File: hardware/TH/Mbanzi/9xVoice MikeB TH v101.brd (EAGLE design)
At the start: 78.1 x 45 mm, 82 parts, among them IC1 ATMEGA328P, IC2 LE33CZ, IC3 LM386N, IC4 LM7805CT, Q1 12MHz, T1 BSS295, T2 BSS295

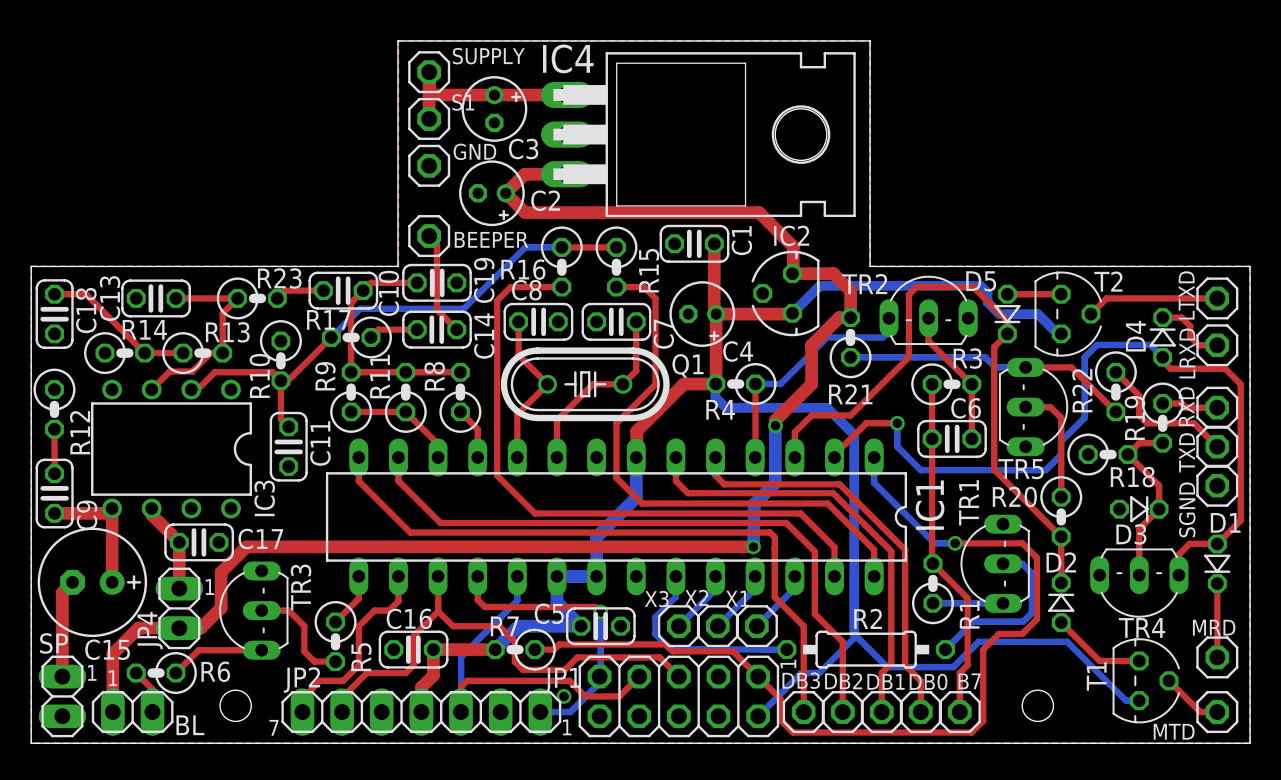
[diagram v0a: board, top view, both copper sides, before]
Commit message: Added Eagle 6.3.0 files for all my versions of the designs
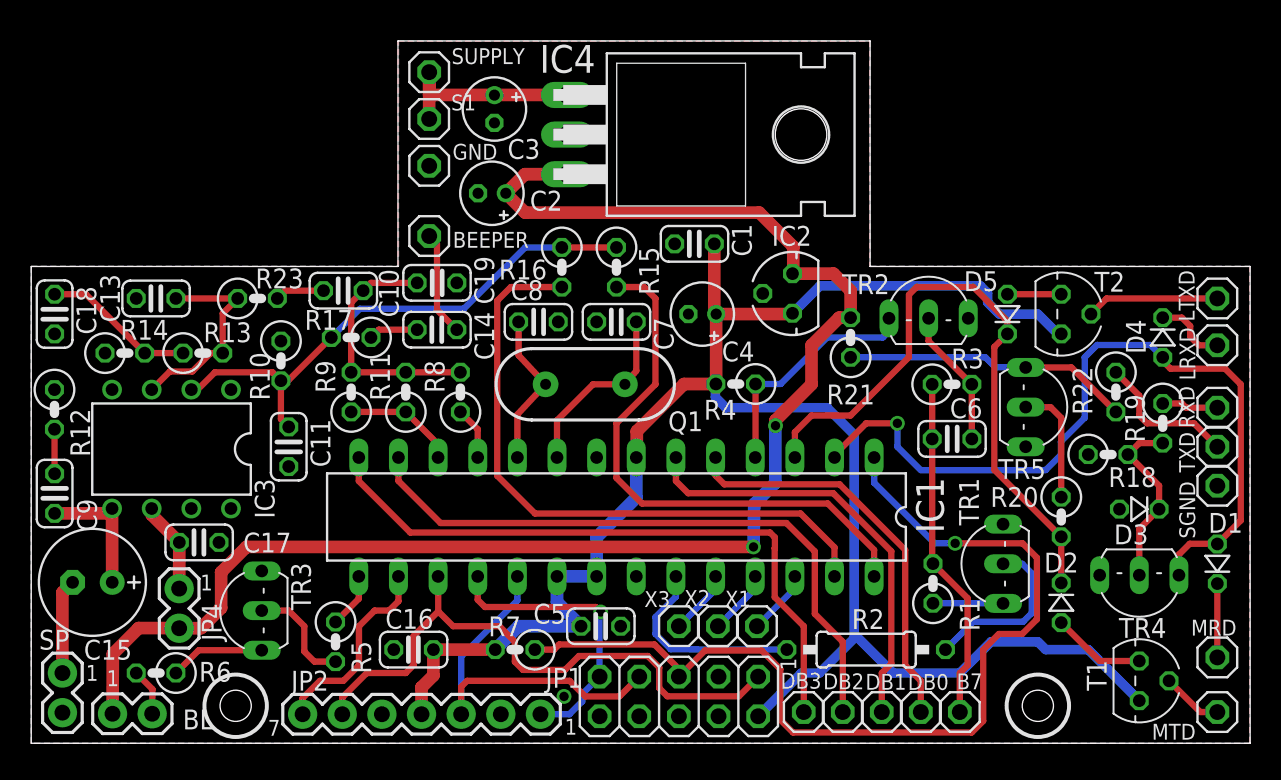
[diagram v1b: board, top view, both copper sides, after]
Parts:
- BL, JP4, SP: device pinhead:1X02 -> SparkFun-Connectors:1X02
- JP2: device pinhead:1X07 -> SparkFun-Connectors:1X07
- Q1: device crystal:HC49/S -> SparkFun-FreqCtrl:HC49US
- moved JP2 7.63 mm to (32.6, 1.86)
- moved SP 1.50 mm to (2.00, 4.50)
- moved BL 1.29 mm to (5.21, 1.89)
- moved JP4 1.27 mm to (9.48, 9.91)
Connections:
- net MOSI: now also JP1.1; no longer JP1.5
- net RESET: now also JP1.5; no longer JP1.1
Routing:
- net MOSI: track 31.3 -> 38.4 mm
- net RESET: track 59.1 -> 61.9 mm
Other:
- board text added: "9xVoice"
- board text added: "v1"
